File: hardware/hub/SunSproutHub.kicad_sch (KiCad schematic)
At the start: 50 parts, among them CN5 1755736, J4 BATTERY, J6 Qwiic, J7 GPIO_HEADER_L, J8 GPIO_HEADER_R, Q1 MDD3415, Q2 DMP3098L-7, Q3 AO3400A, SW1 SW_Push, SW2 SW_Push, U1 ESP32-C5-WROOM-1U

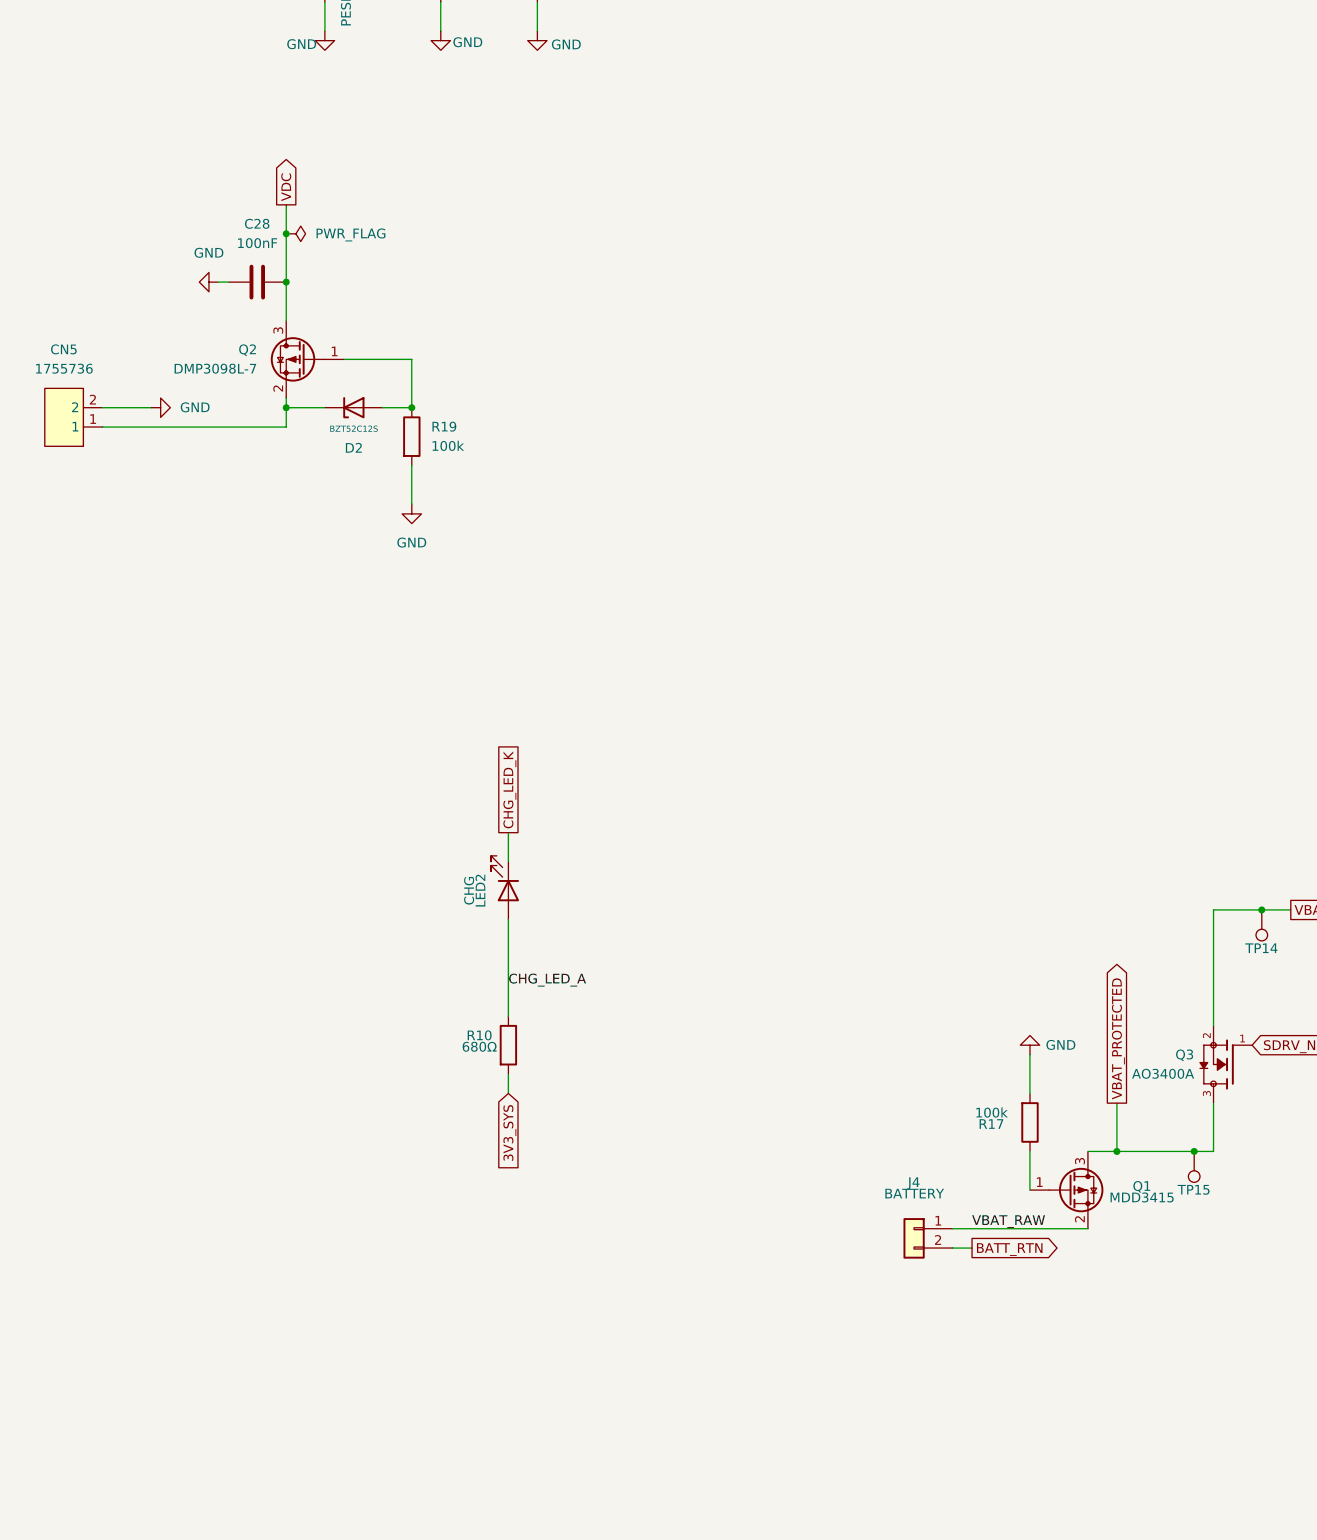
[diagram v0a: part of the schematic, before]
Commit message: fix(hub): turn reverse-polarity FETs Q1/Q2 around so their body diodes block
Q1 and Q2 had their source on the connector and drain on the board. The
gate turned the channel off on a reversed input, but the body diode then
conducted from the board to the connector and dragged VDC / VBAT_PROTECTED
to roughly the reversed voltage, beyond the charger's -2 V VAC/VBUS rating.

- Swap drain and source on Q1 and Q2: drain on J4 / CN5, source on the
  board.
- Move D2's cathode to VDC so it still clamps Q2 gate-to-source.
- Rewrite the topology section of input-protection.md, and update the
  overview and testing-status pages.

Co-Authored-By: Claude Opus 5.5 <noreply@anthropic.com>
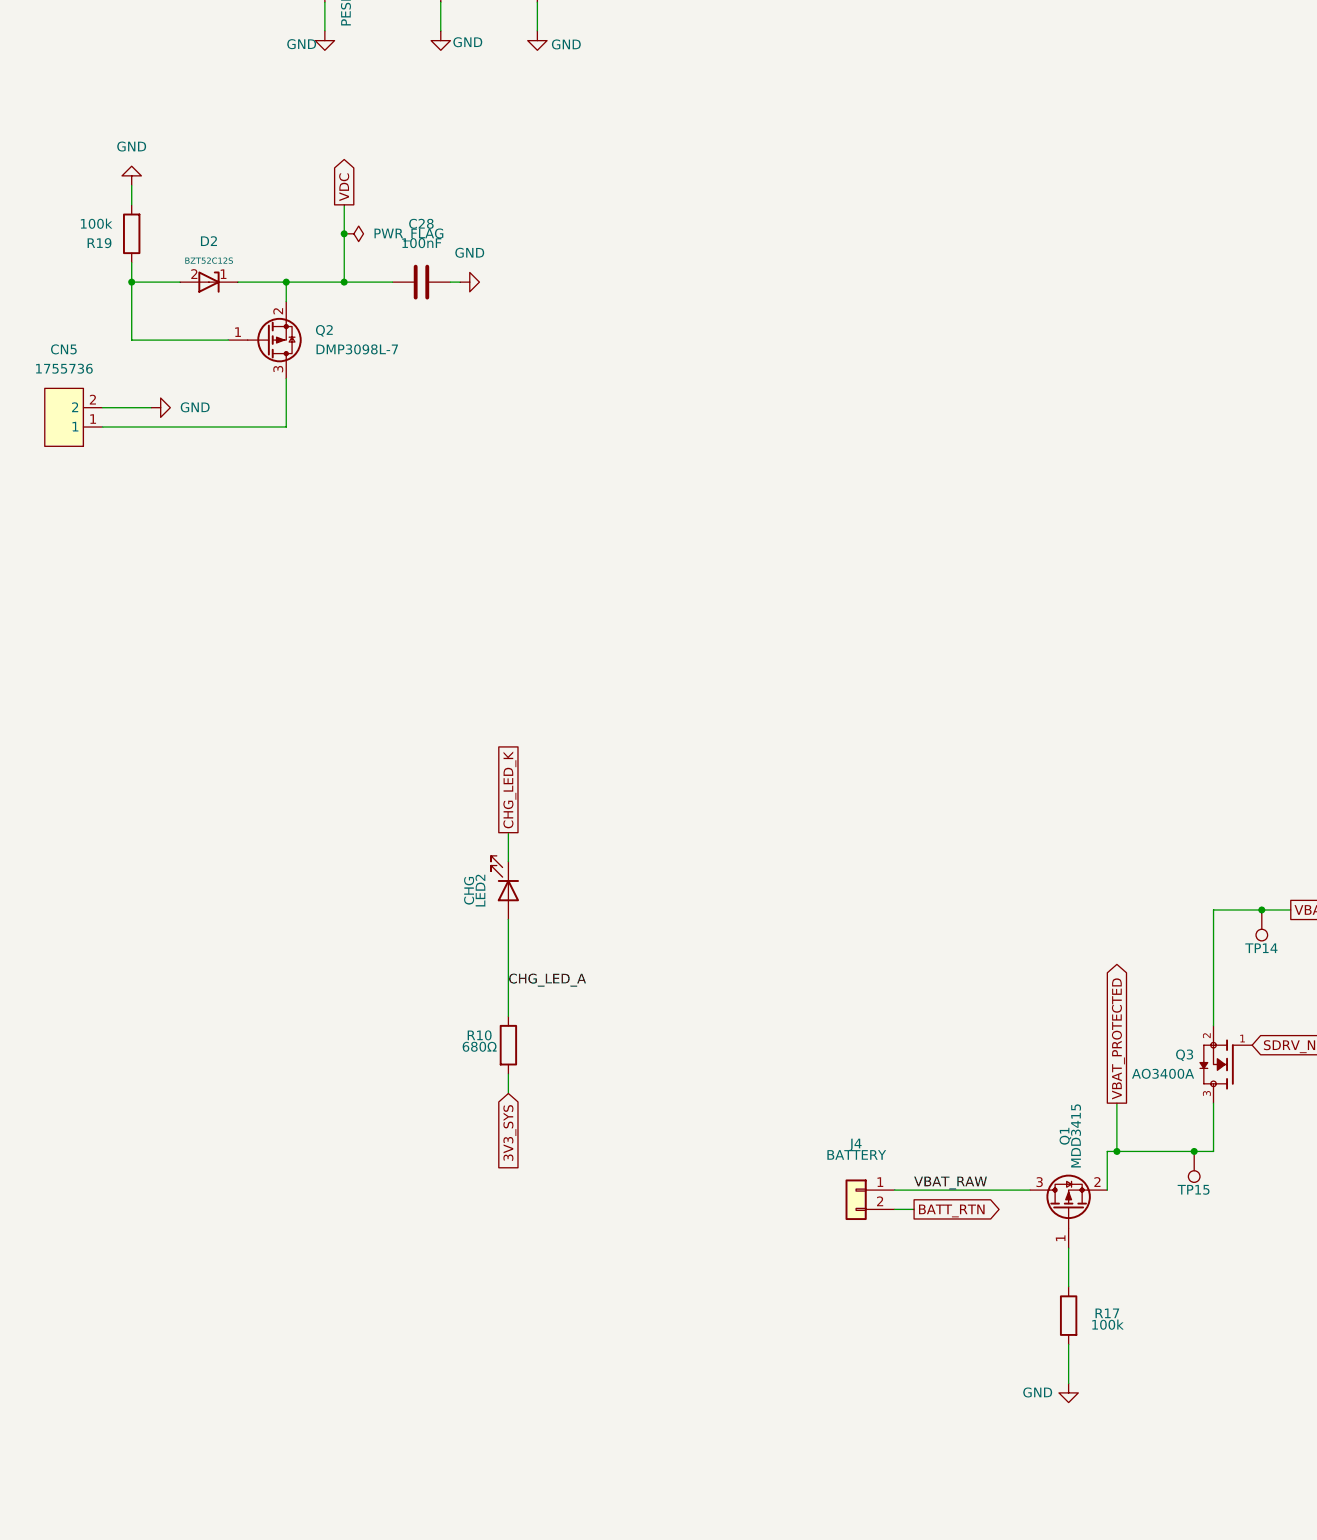
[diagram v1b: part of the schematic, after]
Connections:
- net VBAT_PROTECTED: now also Q1.2 (S); no longer Q1.3 (D)
- net VBAT_RAW: now also Q1.3 (D); no longer Q1.2 (S)
- net VDC: now also D2.1, Q2.2 (S); no longer Q2.3 (D)
- new net: CN5.1, Q2.3 (D)
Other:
- moved on the sheet: C28, J4, Q1, Q2

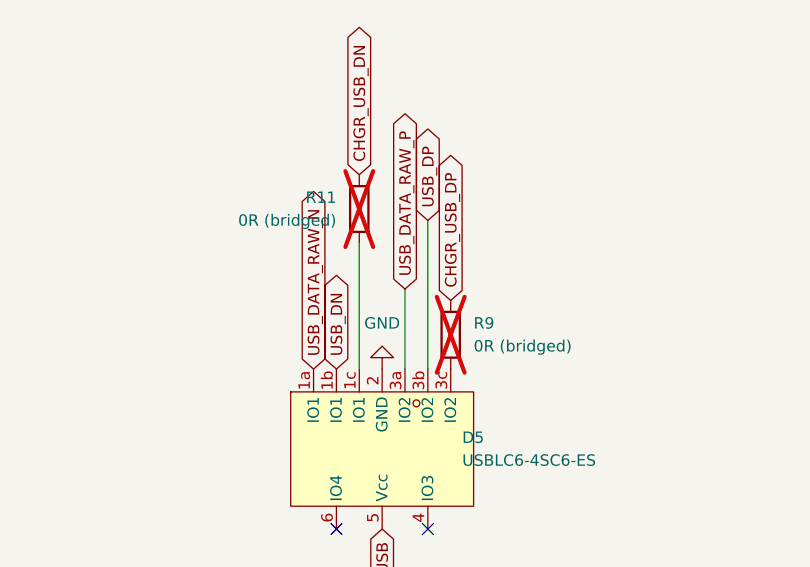
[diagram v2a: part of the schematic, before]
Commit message: hardware(hub): stencil registration, recoloured connector models, wider power traces
- Add F.Paste circles on the four mounting holes so the stencil gets
  registration openings (Ø2.7 mm, matching the holes)
- Recolour 3D models: TS connectors (J302/J401) white, battery (J4) and
  Qwiic (J203/J6) tan, PH pins silver; models live in libraries/3dmodels
  and are referenced via ${KIPRJMOD}; the JST PA footprint now uses the
  repo copy instead of the Snapeda library
- Widen REGN_RAIL/FG_REGIN and several GND segments; Power and Power_2A
  netclass widths raised to 0.4 mm
- R9/R11 switched to R_0603 hand-solder footprint (schematic updated)

Co-Authored-By: Claude Sonnet 5.5 <noreply@anthropic.com>
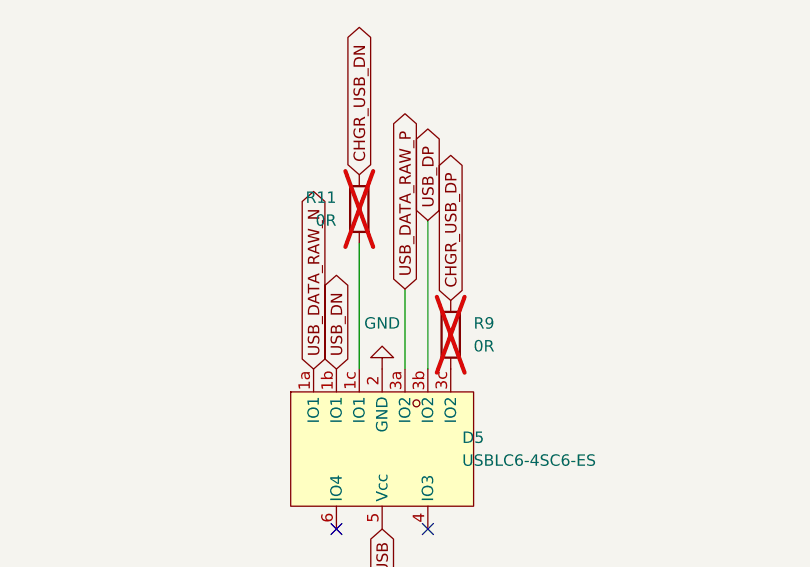
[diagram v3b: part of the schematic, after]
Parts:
- R11: value 0R (bridged) -> 0R; footprint Resistor_SMD:R_0603_1608Metric -> Resistor_SMD:R_0603_1608Metric_Pad0.98x0.95mm_HandSolder; Manufacturer UNI-ROYAL -> (none)
- R9: value 0R (bridged) -> 0R; footprint Resistor_SMD:R_0603_1608Metric -> Resistor_SMD:R_0603_1608Metric_Pad0.98x0.95mm_HandSolder
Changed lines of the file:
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@@
 			)
 		)
-		(property "Value" "0R (bridged)"
+		(property "Value" "0R"
 			(at 180.34 69.8499 0)
 			(show_name no)
@@
 			)
 		)
-		(property "Footprint" "Resistor_SMD:R_0603_1608Metric"
+		(property "Footprint" "Resistor_SMD:R_0603_1608Metric_Pad0.98x0.95mm_HandSolder"
 			(at 177.8 68.58 0)
 			(hide yes)
@@
 			)
 		)
-		(property "Value" "0R (bridged)"
+		(property "Value" "0R"
 			(at 165.1 55.8799 0)
 			(show_name no)
@@
 			)
 		)
-		(property "Footprint" "Resistor_SMD:R_0603_1608Metric"
+		(property "Footprint" "Resistor_SMD:R_0603_1608Metric_Pad0.98x0.95mm_HandSolder"
 			(at 167.64 54.61 0)
 			(hide yes)
@@
 			)
 		)
-		(property "Manufacturer" "UNI-ROYAL"
+		(property "Manufacturer" ""
 			(at 401.32 -120.65 0)
 			(hide yes)
